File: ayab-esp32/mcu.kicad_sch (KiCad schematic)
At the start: 15 parts

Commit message: first draft schematic
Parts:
- removed J?: STDC14_DEBUG, symbol Connector:Conn_ST_STDC14
- removed JP?: JTAG_SEL, symbol Jumper:SolderJumper_3_Bridged12
- removed R? (x2): 10k, symbol Device:R_Small_US
- removed R?: 1k, symbol Device:R_Small_US
- removed SW?: RESET, symbol Switch:SW_Push_45deg
- removed U?: ESP32-S3-WROOM-1, Espressif:ESP32-S3-WROOM-1, symbol Espressif:ESP32-S3-WROOM-1
- added C301, C305: 0.1u, symbol Device:C_Small
- added D301: WS2812B, LED_SMD:LED_WS2812B_PLCC4_5.0x5.0mm_P3.2mm, symbol LED:WS2812B
- added D302: USER0, symbol Device:LED
- added R302: 5.1k, symbol Device:R_Small_US
- added R304, R305, R306: 10k, symbol Device:R_Small_US
- added R307: 0R, symbol Device:R_Small_US
- added SW301: RESET, symbol Switch:SW_Push
- added U301: ESP32-S3-MINI-1, Espressif:ESP32-S3-MINI-1, symbol Espressif:ESP32-S3-MINI-1
- gave numbers to parts that had none: 8
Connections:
- net +3V3: now also R302.1, U301.3 (3V3); no longer BZ301.1 (-)
- net BOOT0: now also U301.4 (GPIO0/BOOT)
- net BOOT1: now also R304.1, U301.44 (GPIO46)
- net BUZZER: now also R306.1, U301.34 (GPIO38/FSPIWP/SUBSPIWP)
- net ENC_A: now also U301.31 (SPIIO6/GPIO35/FSPID/SUBSPID)
- net ENC_B: now also U301.32 (SPIIO7/GPIO36/FSPICLK/SUBSPICLK)
- net ENC_C: now also U301.33 (SPIDQS/GPIO37/FSPIQ/SUBSPIQ)
- net EOL_LEFT: now also U301.5 (GPIO1/TOUCH1/ADC1_CH0)
- net EOL_RIGHT: now also U301.6 (GPIO2/TOUCH2/ADC1_CH1)
- net GND: now also C301.2, C305.2, D301.3 (VSS), R304.2, R305.2, R306.2, SW301.2, U301.1 (GND), U301.2 (GND), U301.42 (GND), U301.43 (GND), U301.46 (GND), U301.47 (GND), U301.48 (GND), U301.49 (GND), U301.50 (GND), U301.51 (GND), U301.52 (GND), U301.53 (GND), U301.54 (GND), U301.55 (GND), U301.56 (GND), U301.57 (GND), U301.58 (GND), U301.59 (GND), U301.60 (GND), U301.61 (GND), U301.62 (GND), U301.63 (GND), U301.64 (GND), U301.65 (GND)
- net I2C_SCL: now also U301.30 (GPIO48/SPICLK_N/SUBSPICLK_N_DIFF)
- net I2C_SDA: now also U301.27 (GPIO47/SPICLK_P/SUBSPICLK_P_DIFF)
- net MCU_SOL_0: now also U301.8 (GPIO4/TOUCH4/ADC1_CH3)
- net MCU_SOL_1: now also U301.9 (GPIO5/TOUCH5/ADC1_CH4)
- net MCU_SOL_2: now also U301.10 (GPIO6/TOUCH6/ADC1_CH5)
- net MCU_SOL_3: now also U301.11 (GPIO7/TOUCH7/ADC1_CH6)
- net MCU_SOL_4: now also U301.19 (GPIO15/U0RTS/ADC2_CH4/XTAL_32K_P)
- net MCU_SOL_5: now also U301.20 (GPIO16/U0CTS/ADC2_CH5/XTAL_32K_N)
- net MCU_SOL_6: now also U301.21 (GPIO17/U1TXD/ADC2_CH6)
- net MCU_SOL_7: now also U301.22 (GPIO18/U1RXD/ADC2_CH7/CLK_OUT3)
- net MCU_SOL_8: now also U301.12 (GPIO8/TOUCH8/ADC1_CH7/SUBSPICS1)
- net MCU_SOL_9: now also U301.13 (GPIO9/TOUCH9/ADC1_CH8/FSPIHD/SUBSPIHD)
- net MCU_SOL_A: now also U301.14 (GPIO10/TOUCH10/ADC1_CH9/FSPICS0/FSPIIO4/SUBSPICS0)
- net MCU_SOL_B: now also U301.15 (GPIO11/TOUCH11/ADC2_CH0/FSPID/FSPIIO5/SUBSPID)
- net MCU_SOL_C: now also U301.16 (GPIO12/TOUCH12/ADC2_CH1/FSPICLK/FSPIIO6/SUBSPICLK)
- net MCU_SOL_D: now also U301.17 (GPIO13/TOUCH13/ADC2_CH2/FSPIQ/FSPIIO7/SUBSPIQ)
- net MCU_SOL_E: now also U301.18 (GPIO14/TOUCH14/ADC2_CH3/FSPIWP/FSPIDQS/SUBSPIWP)
- net MCU_SOL_F: now also U301.25 (GPIO21)
- net USB_M: now also U301.23 (GPIO19/U1RTS/ADC2_CH8/CLK_OUT2/USB_D-)
- net USB_P: now also U301.24 (GPIO20/U1CTS/ADC2_CH9/CLK_OUT1/USB_D+)
- net VCC_SPI: now also R305.1, U301.41 (GPIO45)
- net nRST: now also C301.1, SW301.1, U301.45 (EN)
- net at Q301.3 (D): now also R307.2; no longer BZ301.2 (+)
- new net: D302.1 (K), U301.28 (SPIIO4/GPIO33/FSPIHD/SUBSPIHD)
- new net: D301.4 (DIN), U301.35 (MTCK/GPIO39/CLK_OUT3/SUBSPICS1)
- new net: D302.2 (A), R302.2
- new net: BZ301.2 (+), R307.1
- new net +5V: BZ301.1 (-), C305.1, D301.1 (VDD)
- new net EOL_R_LC: U301.7 (GPIO3/TOUCH3/ADC1_CH2)
- new net SPI_CIPO: U301.37 (MTDI/GPIO41/CLK_OUT1)
- new net SPI_COPI: U301.36 (MTDO/GPIO40/CLK_OUT2)
- new net SPI_CS: U301.38 (MTMS/GPIO42)
- new net UART_RX: U301.40 (U0RXD/GPIO44/CLK_OUT2)
- new net UART_TX: U301.39 (U0TXD/GPIO43/CLK_OUT1)
- new net USB_VBUS: U301.29 (SPIIO5/GPIO34/FSPICS0/SUBSPICS0)
- no-connect marks 1 -> 3
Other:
- note added: "RESET"
- company: (none) -> matei
- title: (none) -> ESP32
- moved on the sheet: BZ301, Q301, R301, R303, SW302

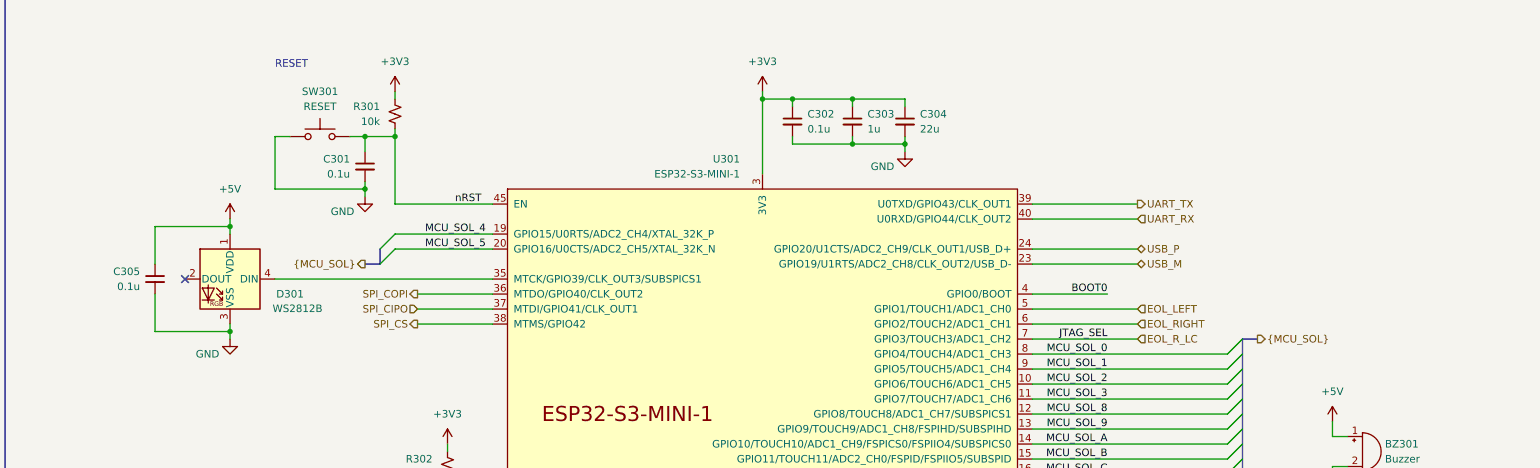
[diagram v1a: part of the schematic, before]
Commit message: add spi_sck line
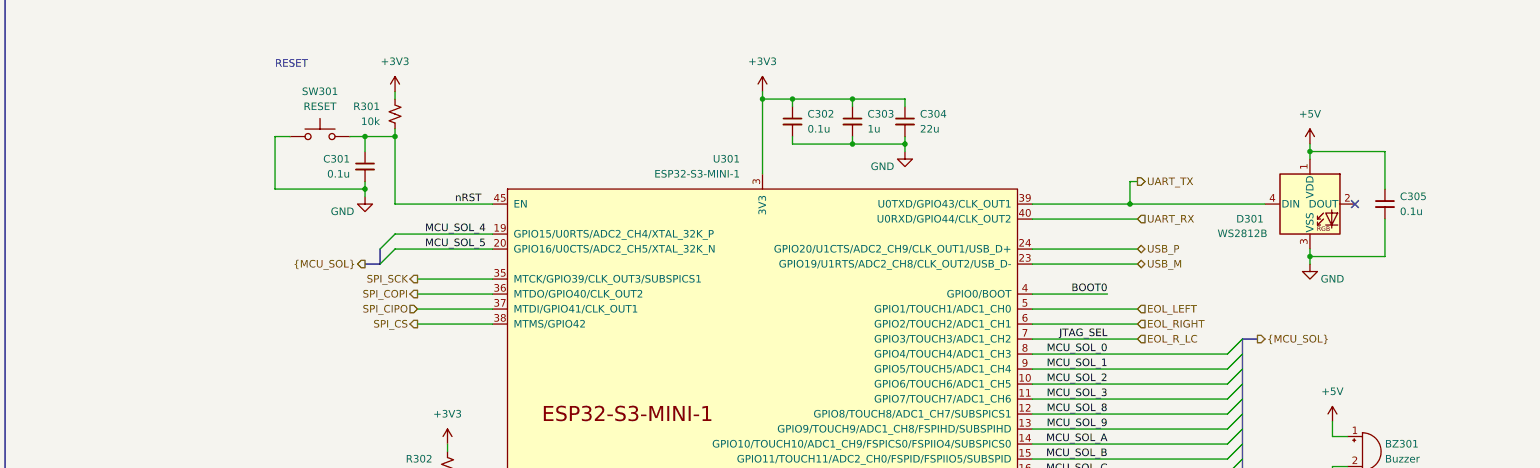
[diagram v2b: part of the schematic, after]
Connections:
- net UART_TX: now also D301.4 (DIN)
- net SPI_SCK: now reaches U301.35 (MTCK/GPIO39/CLK_OUT3/SUBSPICS1)
- net SPI_SCK: no longer D301.4 (DIN)
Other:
- moved on the sheet: C305, D301
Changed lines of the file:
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@@
     (comment 2 "distributed under CC-BY-SA-4.0")
   )
-  (junction (at 54.61 76.2) (diameter 0) (color 0 0 0 0)
+  (junction (at 237.49 63.5) (diameter 0) (color 0 0 0 0)
   )
   (junction (at 82.55 43.18) (diameter 0) (color 0 0 0 0)
@@
   (junction (at 77.47 52.07) (diameter 0) (color 0 0 0 0)
   )
-  (junction (at 54.61 58.42) (diameter 0) (color 0 0 0 0)
+  (junction (at 237.49 45.72) (diameter 0) (color 0 0 0 0)
   )
   (junction (at 107.95 184.15) (diameter 0) (color 0 0 0 0)
@@
   (junction (at 149.86 36.83) (diameter 0) (color 0 0 0 0)
   )
+  (junction (at 207.01 54.61) (diameter 0) (color 0 0 0 0)
+  )
   (junction (at 77.47 43.18) (diameter 0) (color 0 0 0 0)
   )
@@
   (no_connect (at 99.06 113.03))
   (no_connect (at 50.8 177.8))
-  (no_connect (at 46.99 67.31))
+  (no_connect (at 245.11 54.61))
   (bus_entry (at 80.01 64.77) (size 2.54 -2.54)
     (stroke (width 0) (type default))
@@
     (stroke (width 0) (type default))
   )
-  (wire (pts (xy 41.91 76.2) (xy 54.61 76.2))
+  (wire (pts (xy 250.19 63.5) (xy 237.49 63.5))
     (stroke (width 0) (type default))
   )
@@
     (stroke (width 0) (type default))
   )
-  (wire (pts (xy 41.91 58.42) (xy 41.91 64.77))
+  (wire (pts (xy 250.19 45.72) (xy 250.19 52.07))
     (stroke (width 0) (type default))
   )
@@
     (stroke (width 0) (type default))
   )
-  (wire (pts (xy 54.61 58.42) (xy 41.91 58.42))
+  (wire (pts (xy 237.49 45.72) (xy 250.19 45.72))
     (stroke (width 0) (type default))
   )
@@
     (stroke (width 0) (type default))
   )
-  (wire (pts (xy 62.23 67.31) (xy 99.06 67.31))
+  (polyline (pts (xy 16.51 158.75) (xy 172.72 158.75))
     (stroke (width 0) (type default))
   )
-  (polyline (pts (xy 16.51 158.75) (xy 172.72 158.75))
+  (wire (pts (xy 207.01 54.61) (xy 190.5 54.61))
     (stroke (width 0) (type default))
   )
@@
     (stroke (width 0) (type default))
   )
-  (wire (pts (xy 41.91 69.85) (xy 41.91 76.2))
+  (wire (pts (xy 250.19 57.15) (xy 250.19 63.5))
     (stroke (width 0) (type default))
   )
-  (wire (pts (xy 54.61 57.15) (xy 54.61 58.42))
+  (wire (pts (xy 237.49 44.45) (xy 237.49 45.72))
     (stroke (width 0) (type default))
   )
@@
     (stroke (width 0) (type default))
   )
+  (wire (pts (xy 207.01 54.61) (xy 229.87 54.61))
+    (stroke (width 0) (type default))
+  )
   (wire (pts (xy 64.77 43.18) (xy 62.23 43.18))
     (stroke (width 0) (type default))
@@
     (stroke (width 0) (type default))
   )
-  (wire (pts (xy 190.5 54.61) (xy 208.28 54.61))
+  (wire (pts (xy 207.01 50.8) (xy 208.28 50.8))
     (stroke (width 0) (type default))
   )
@@
     (stroke (width 0) (type default))
   )
-  (wire (pts (xy 54.61 76.2) (xy 54.61 77.47))
+  (wire (pts (xy 237.49 63.5) (xy 237.49 64.77))
     (stroke (width 0) (type default))
   )
@@
     (stroke (width 0) (type default))
   )
-  (wire (pts (xy 54.61 74.93) (xy 54.61 76.2))
+  (wire (pts (xy 237.49 62.23) (xy 237.49 63.5))
     (stroke (width 0) (type default))
   )
@@
     (stroke (width 0) (type default))
   )
+  (wire (pts (xy 207.01 50.8) (xy 207.01 54.61))
+    (stroke (width 0) (type default))
+  )
   (wire (pts (xy 77.47 50.8) (xy 77.47 52.07))
     (stroke (width 0) (type default))
@@
     (stroke (width 0) (type default))
   )
-  (wire (pts (xy 54.61 58.42) (xy 54.61 59.69))
+  (wire (pts (xy 237.49 45.72) (xy 237.49 46.99))
     (stroke (width 0) (type default))
   )
@@
     (stroke (width 0) (type default))
   )
+  (wire (pts (xy 86.36 67.31) (xy 99.06 67.31))
+    (stroke (width 0) (type default))
+  )
   (bus (pts (xy 226.06 100.33) (xy 226.06 102.87))
     (stroke (width 0) (type default))
@@
     (effects (font (size 1.27 1.27)) (justify right))
   )
-  (hierarchical_label "UART_TX" (shape output) (at 208.28 54.61 0) (fields_autoplaced)
+  (hierarchical_label "UART_TX" (shape output) (at 208.28 50.8 0) (fields_autoplaced)
     (effects (font (size 1.27 1.27)) (justify left))
   )
@@
     (effects (font (size 1.27 1.27)) (justify left))
   )
+  (hierarchical_label "SPI_SCK" (shape output) (at 86.36 67.31 180) (fields_autoplaced)
+    (effects (font (size 1.27 1.27)) (justify right))
+  )
   (hierarchical_label "EOL_LEFT" (shape input) (at 208.28 72.39 0) (fields_autoplaced)
     (effects (font (size 1.27 1.27)) (justify left))
@@
     )
   )
-  (symbol (lib_id "LED:WS2812B") (at 54.61 67.31 0) (mirror y) (unit 1)
+  (symbol (lib_id "LED:WS2812B") (at 237.49 54.61 0) (unit 1)
     (in_bom yes) (on_board yes) (dnp no)
-    (property "Reference" "D301" (at 64.77 69.85 0)
+    (property "Reference" "D301" (at 227.33 57.15 0)
       (effects (font (size 1.27 1.27)))
     )
-    (property "Value" "WS2812B" (at 66.04 72.3139 0)
+    (property "Value" "WS2812B" (at 226.06 59.6139 0)
       (effects (font (size 1.27 1.27)))
     )
-    (property "Footprint" "LED_SMD:LED_WS2812B_PLCC4_5.0x5.0mm_P3.2mm" (at 53.34 74.93 0)
+    (property "Footprint" "LED_SMD:LED_WS2812B_PLCC4_5.0x5.0mm_P3.2mm" (at 238.76 62.23 0)
       (effects (font (size 1.27 1.27)) (justify left top) hide)
     )
-    (property "Datasheet" "https://cdn-shop.adafruit.com/datasheets/WS2812B.pdf" (at 52.07 76.835 0)
+    (property "Datasheet" "https://cdn-shop.adafruit.com/datasheets/WS2812B.pdf" (at 240.03 64.135 0)
       (effects (font (size 1.27 1.27)) (justify left top) hide)
     )
@@
     )
   )
-  (symbol (lib_id "power:GND") (at 54.61 77.47 0) (unit 1)
+  (symbol (lib_id "power:GND") (at 237.49 64.77 0) (mirror y) (unit 1)
     (in_bom yes) (on_board yes) (dnp no)
-    (property "Reference" "#PWR013" (at 54.61 83.82 0)
+    (property "Reference" "#PWR013" (at 237.49 71.12 0)
       (effects (font (size 1.27 1.27)) hide)
     )
-    (property "Value" "GND" (at 50.8 80.01 0)
+    (property "Value" "GND" (at 241.3 67.31 0)
       (effects (font (size 1.27 1.27)))
     )
-    (property "Footprint" "" (at 54.61 77.47 0)
+    (property "Footprint" "" (at 237.49 64.77 0)
       (effects (font (size 1.27 1.27)) hide)
     )
-    (property "Datasheet" "" (at 54.61 77.47 0)
+    (property "Datasheet" "" (at 237.49 64.77 0)
       (effects (font (size 1.27 1.27)) hide)
     )
@@
     )
   )
-  (symbol (lib_id "Device:C_Small") (at 41.91 67.31 0) (mirror y) (unit 1)
+  (symbol (lib_id "Device:C_Small") (at 250.19 54.61 0) (unit 1)
     (in_bom yes) (on_board yes) (dnp no)
-    (property "Reference" "C305" (at 39.37 66.0463 0)
+    (property "Reference" "C305" (at 252.73 53.3463 0)
       (effects (font (size 1.27 1.27)) (justify left))
     )
-    (property "Value" "0.1u" (at 39.37 68.5863 0)
+    (property "Value" "0.1u" (at 252.73 55.8863 0)
       (effects (font (size 1.27 1.27)) (justify left))
     )
-    (property "Footprint" "" (at 41.91 67.31 0)
+    (property "Footprint" "" (at 250.19 54.61 0)
       (effects (font (size 1.27 1.27)) hide)
     )
-    (property "Datasheet" "~" (at 41.91 67.31 0)
+    (property "Datasheet" "~" (at 250.19 54.61 0)
       (effects (font (size 1.27 1.27)) hide)
     )
@@
     )
   )
-  (symbol (lib_id "power:+5V") (at 54.61 57.15 0) (unit 1)
+  (symbol (lib_id "power:+5V") (at 237.49 44.45 0) (mirror y) (unit 1)
     (in_bom yes) (on_board yes) (dnp no) (fields_autoplaced)
-    (property "Reference" "#PWR06" (at 54.61 60.96 0)
+    (property "Reference" "#PWR06" (at 237.49 48.26 0)
       (effects (font (size 1.27 1.27)) hide)
     )
-    (property "Value" "+5V" (at 54.61 52.07 0)
+    (property "Value" "+5V" (at 237.49 39.37 0)
       (effects (font (size 1.27 1.27)))
     )
-    (property "Footprint" "" (at 54.61 57.15 0)
+    (property "Footprint" "" (at 237.49 44.45 0)
       (effects (font (size 1.27 1.27)) hide)
     )
-    (property "Datasheet" "" (at 54.61 57.15 0)
+    (property "Datasheet" "" (at 237.49 44.45 0)
       (effects (font (size 1.27 1.27)) hide)
     )

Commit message: fix some comments from jpcornil-git
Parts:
- removed D302: USER0, symbol Device:LED
- removed R302: 5.1k, symbol Device:R_Small_US
- added R?: 20k, symbol Device:R_Small_US
- added R?: 30k, symbol Device:R_Small_US
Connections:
- net GND: now also R?.2
- net I2C_SDA: now also U301.29 (SPIIO5/GPIO34/FSPICS0/SUBSPICS0); no longer U301.27 (GPIO47/SPICLK_P/SUBSPICLK_P_DIFF)
- net USB_VBUS: now also R?.2; no longer U301.29 (SPIIO5/GPIO34/FSPICS0/SUBSPICS0)
- net EOL_R_S: now reaches U301.28 (SPIIO4/GPIO33/FSPIHD/SUBSPIHD)
- net EOL_R_LC: no longer names the net of U301.7 (GPIO3/TOUCH3/ADC1_CH2)
- net EOL_R_LC: now also R?.1, R?.1
- new net EOL_R_N: U301.27 (GPIO47/SPICLK_P/SUBSPICLK_P_DIFF)
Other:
- moved on the sheet: BZ301, C301, C302, C303, C304, C305, D301, Q301, R301, R306, R307, SW301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

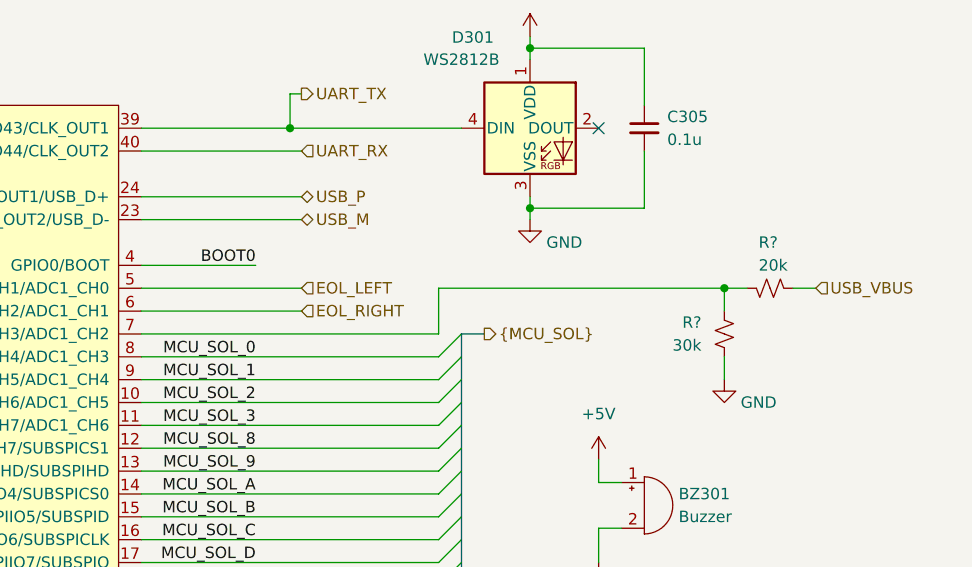
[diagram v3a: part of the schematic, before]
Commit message: add pch MOSFET for polarity protection
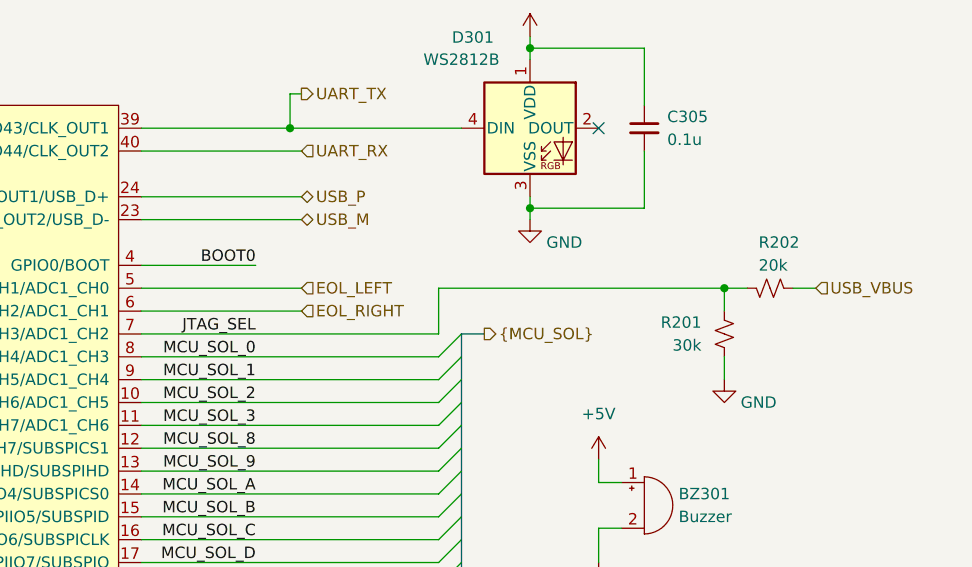
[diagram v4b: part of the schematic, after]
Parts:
- gave numbers to parts that had none: 2
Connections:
- net JTAG_SEL: now also R201.1, R202.1, U301.7 (GPIO3/TOUCH3/ADC1_CH2)
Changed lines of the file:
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@@
+    (effects (font (size 1.27 1.27)) (justify right bottom))
+  )
+  (label "JTAG_SEL" (at 189.23 78.74 180) (fields_autoplaced)
     (effects (font (size 1.27 1.27)) (justify right bottom))
   )
@@
   (symbol (lib_id "Device:R_Small_US") (at 246.38 73.66 90) (mirror x) (unit 1)
     (in_bom yes) (on_board yes) (dnp no)
-    (property "Reference" "R?" (at 245.11 68.58 90)
+    (property "Reference" "R202" (at 245.11 68.58 90)
       (effects (font (size 1.27 1.27)) (justify right))
     )
@@
       (project "ayab-esp32"
         (path "/ad16b75f-afc8-4717-a7c6-8dd7b69a18e2/a7e0db0f-e473-44d4-a2fe-681f732aacb2"
-          (reference "R?") (unit 1)
+          (reference "R202") (unit 1)
         )
       )
@@
   (symbol (lib_id "Device:R_Small_US") (at 241.3 78.74 0) (unit 1)
     (in_bom yes) (on_board yes) (dnp no)
-    (property "Reference" "R?" (at 238.76 77.47 0)
+    (property "Reference" "R201" (at 238.76 77.47 0)
       (effects (font (size 1.27 1.27)) (justify right))
     )
@@
       (project "ayab-esp32"
         (path "/ad16b75f-afc8-4717-a7c6-8dd7b69a18e2/a7e0db0f-e473-44d4-a2fe-681f732aacb2"
-          (reference "R?") (unit 1)
-        )
-      )
+          (reference "R201") (unit 1)
+        )
+      )
